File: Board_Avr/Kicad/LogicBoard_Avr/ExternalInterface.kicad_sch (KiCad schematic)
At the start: 5 parts, among them J5 SPI Connector, J6 ICSP Header, J7 I2C Connector, J8 UART Connector, J9 GPIO Header

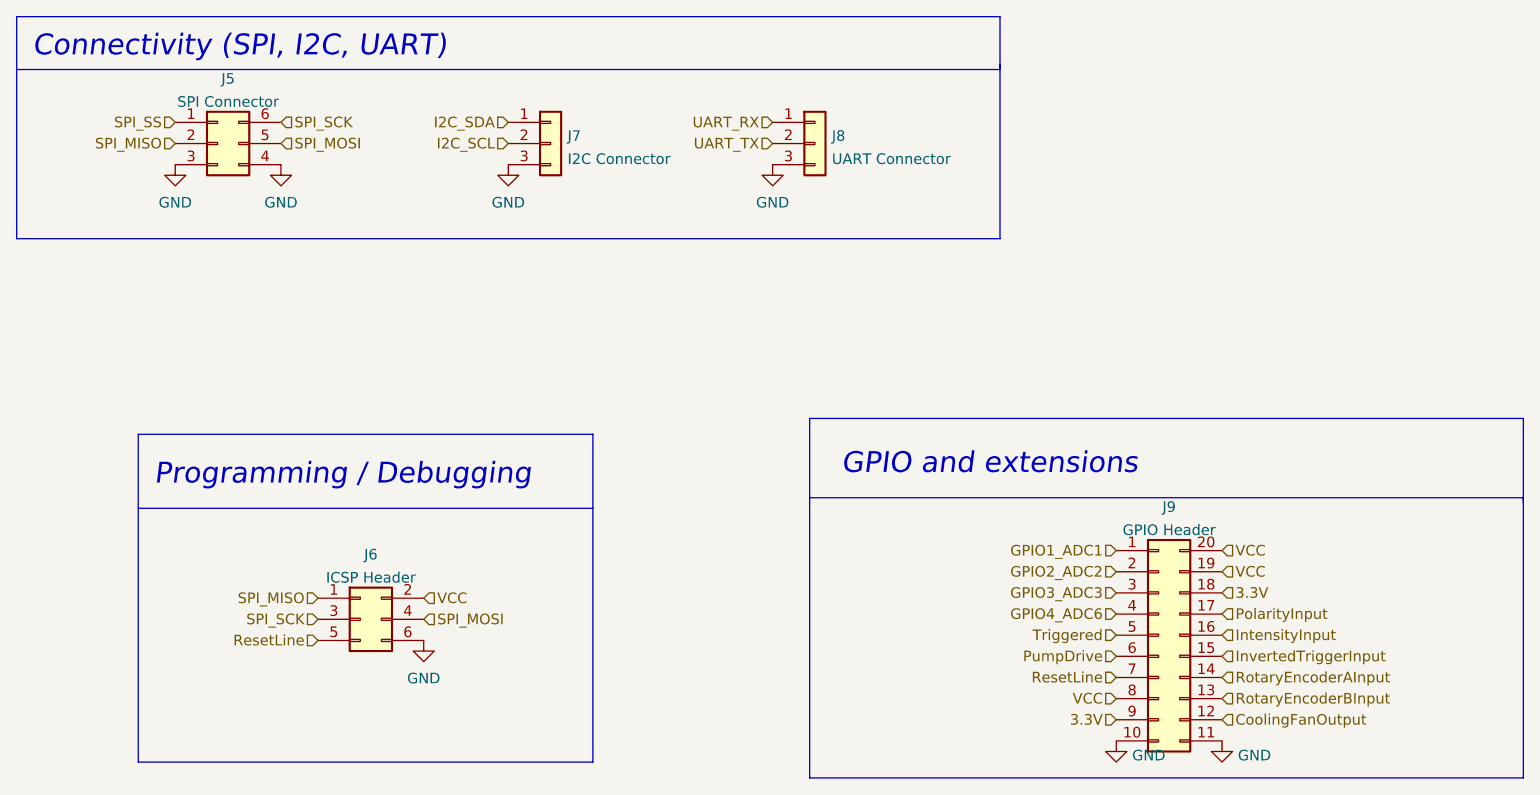
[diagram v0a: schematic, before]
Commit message: Fixed misorganised pins and updated pin mapping table
Signed-off-by: bebenlebricolo <benoittarrade@hotmail.fr>
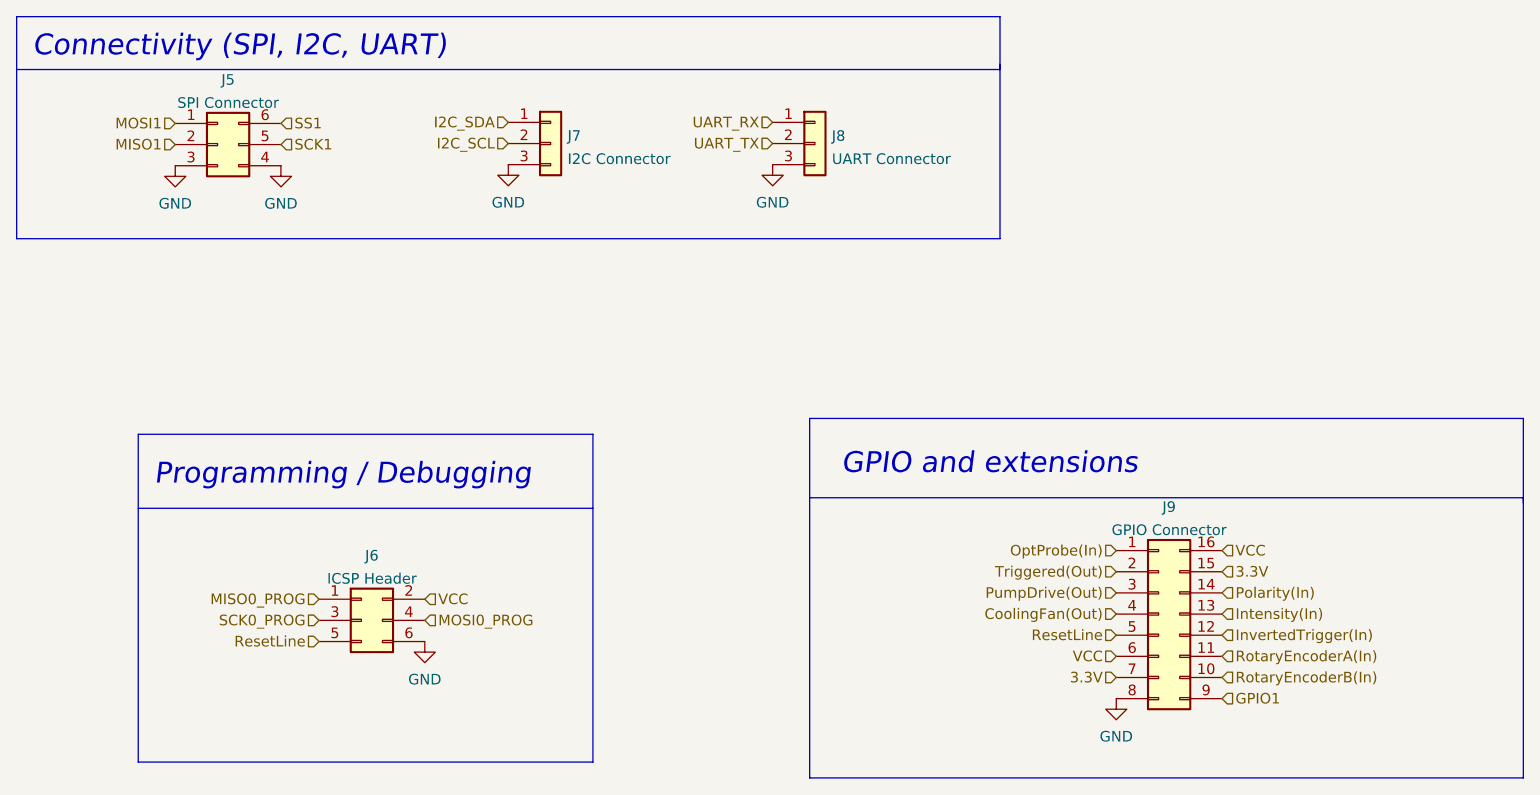
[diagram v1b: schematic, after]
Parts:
- removed J9: GPIO Header, symbol Connector_Generic:Conn_02x10_Counter_Clockwise
- added J9: GPIO Connector, symbol Connector_Generic:Conn_02x08_Counter_Clockwise
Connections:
- net 3.3V: now also J9.15 (Pin_15), J9.7 (Pin_7)
- net GND: now also J9.8 (Pin_8)
- net ResetLine: now also J9.5 (Pin_5)
- net VCC: now also J9.16 (Pin_16), J9.6 (Pin_6)
- net SPI_MISO renamed MISO0_PROG
- net MISO0_PROG: no longer J5.2 (Pin_2)
- net SPI_MOSI renamed MOSI0_PROG
- net MOSI0_PROG: no longer J5.5 (Pin_5)
- net SPI_SCK renamed SCK0_PROG
- net SCK0_PROG: no longer J5.6 (Pin_6)
- net SPI_SS renamed MOSI1
- new net CoolingFan(Out): J9.4 (Pin_4)
- new net GPIO1: J9.9 (Pin_9)
- new net Intensity(In): J9.13 (Pin_13)
- new net InvertedTrigger(In): J9.12 (Pin_12)
- new net MISO1: J5.2 (Pin_2)
- new net OptProbe(In): J9.1 (Pin_1)
- new net Polarity(In): J9.14 (Pin_14)
- new net PumpDrive(Out): J9.3 (Pin_3)
- new net RotaryEncoderA(In): J9.11 (Pin_11)
- new net RotaryEncoderB(In): J9.10 (Pin_10)
- new net SCK1: J5.5 (Pin_5)
- new net SS1: J5.6 (Pin_6)
- new net Triggered(Out): J9.2 (Pin_2)

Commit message: Started routing all traces
Signed-off-by: bebenlebricolo <benoittarrade@hotmail.fr>
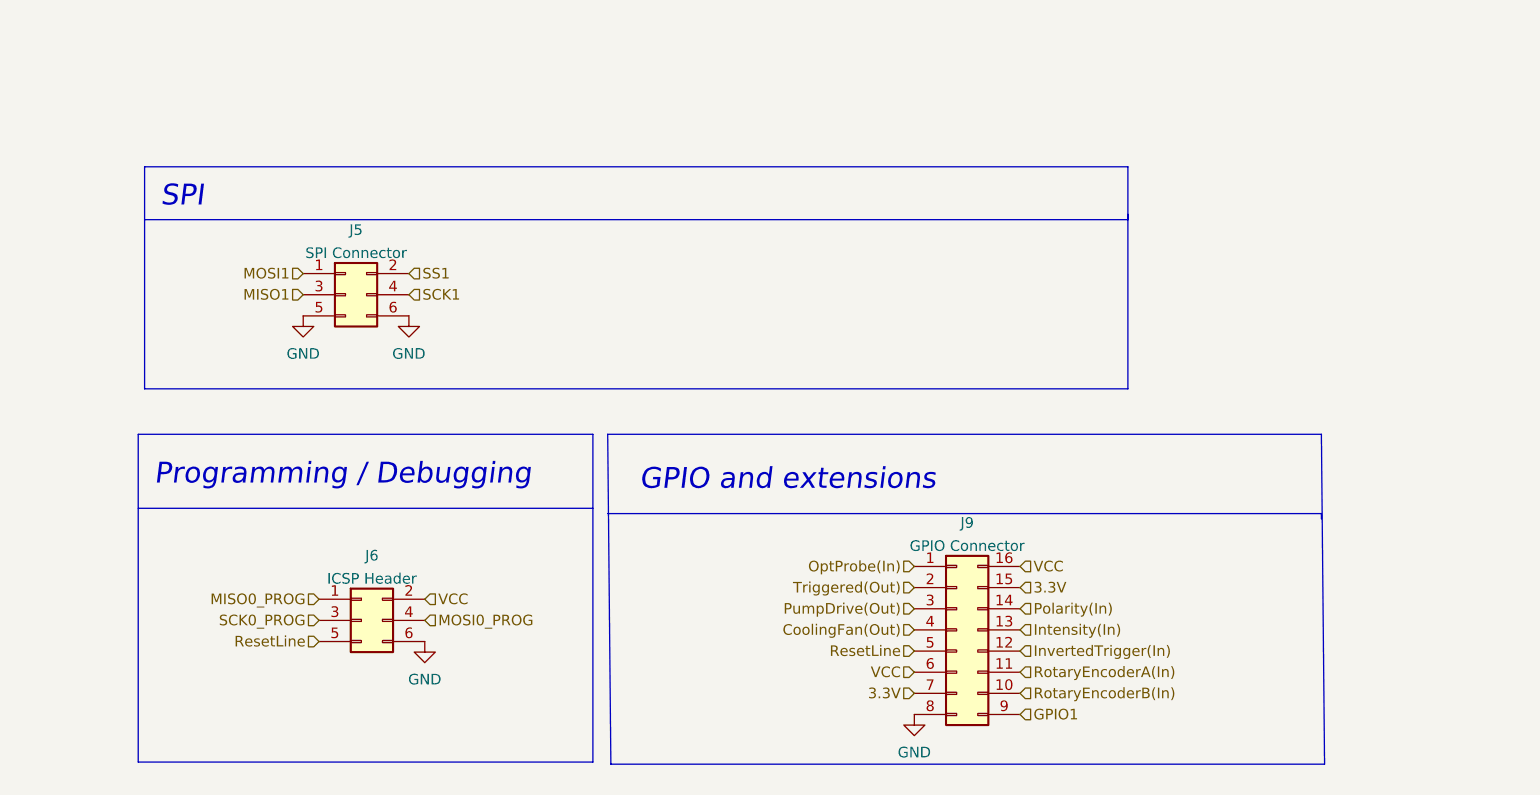
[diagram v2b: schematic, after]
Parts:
- removed J7: I2C Connector, symbol Connector_Generic:Conn_01x03
- removed J8: UART Connector, symbol Connector_Generic:Conn_01x03
- J5: footprint (none) -> Connector_PinHeader_2.54mm:PinHeader_2x03_P2.54mm_Vertical; symbol Connector_Generic:Conn_02x03_Counter_Clockwise -> Connector_Generic:Conn_02x03_Odd_Even
- J6: footprint (none) -> Connector_PinHeader_2.54mm:PinHeader_2x03_P2.54mm_Vertical
- J9: footprint (none) -> Connector_PinHeader_2.54mm:PinHeader_2x08_P2.54mm_Vertical
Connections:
- net GND: now also J5.5 (Pin_5), J5.6 (Pin_6); no longer J5.3 (Pin_3), J5.4 (Pin_4)
- net MISO1: now also J5.3 (Pin_3); no longer J5.2 (Pin_2)
- net SCK1: now also J5.4 (Pin_4); no longer J5.5 (Pin_5)
- net SS1: now also J5.2 (Pin_2); no longer J5.6 (Pin_6)
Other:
- note added: "SPI"
- note removed: "Connectivity (SPI, I2C, UART)"
- moved on the sheet: J5, J9
